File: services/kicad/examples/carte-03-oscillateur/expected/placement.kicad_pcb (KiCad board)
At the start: 2 copper layers, 27.8 x 19.8 mm, 15 parts, among them J1 PWR, J2 OUT, U1 NE555

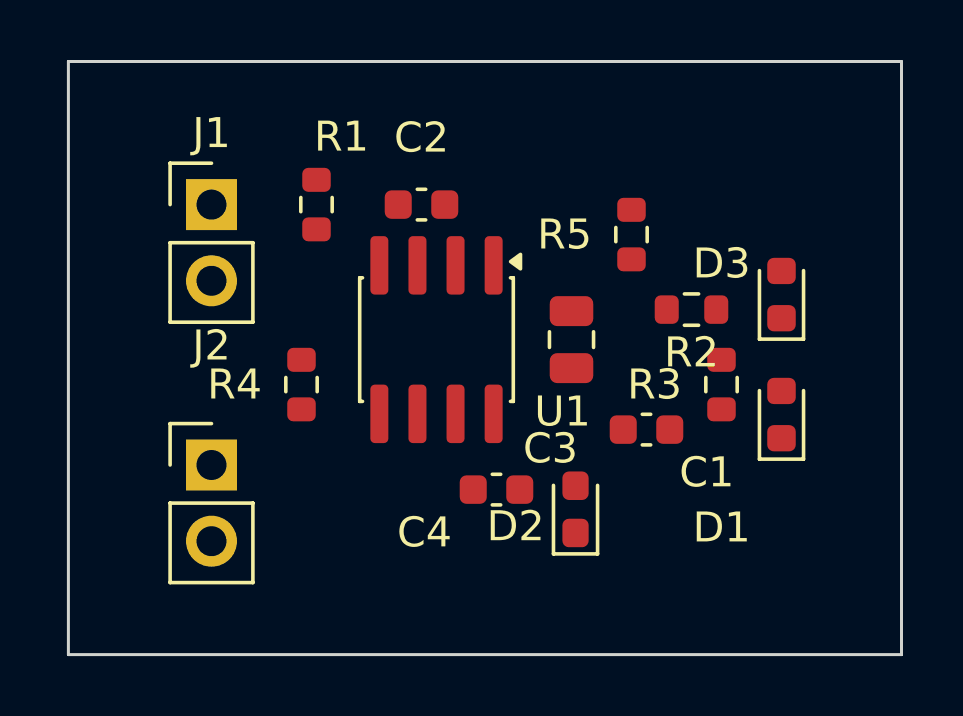
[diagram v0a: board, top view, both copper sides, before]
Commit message: feat(placement): les peripheriques se REPARTISSENT, ils ne s empilent plus
Question de l utilisateur devant le rendu : « c est quoi ce type de placement ? ».
Les composants s entassaient d un seul cote du boitier, etiquettes de
serigraphie l une sur l autre, trois quarts de la couronne vides.

TROIS CAUSES, toutes dans `_poser_les_peripheriques`, toutes la meme faute —
un angle unique pour tout un groupe :

  - les DIRECTS qui visent la meme broche (tous les decouplages d un rail,
    toutes les resistances d un meme signal) recevaient le MEME `angle_vers`
    et le meme rayon de depart ;
  - les SUIVEURS d un meme parent recevaient tous atan2(parent - centre) ;
  - les ISOLES partaient tous de l angle 0.0, c est-a-dire du meme point.

`le_long_du_rayon` ne s ecartait qu une fois la place prise : d ou la file.

REMEDE : `_ecart_en_eventail`. Le PREMIER de chaque groupe garde EXACTEMENT la
direction calculee — c est la topologie, on ne la perd pas pour faire joli — et
les suivants s ecartent symetriquement de 3 x `_PAS_ANGLE_DEG`.
Rien de deja pose ne bouge : seul l ANGLE DE DEPART de la recherche change, et
`le_long_du_rayon` reste seul juge de ce qui est libre.

BANC DES DIX CARTES, contour resserre ET peripheriques repartis :

    carte             demandee    livree         err  manq
    carte-01           25 x 20    20,1 x 13,6     0    0
    carte-02           55 x 40    34,9 x 25,2     0    0
    carte-03           50 x 35    27,6 x 19,9     0    0
    carte-04           60 x 45    36,6 x 29,8     0    0
    carte-05           70 x 50    40,0 x 32,6     0    0
    carte-06           80 x 60    46,5 x 36,4     0    0
    carte-07          110 x 80    47,7 x 38,8     0    0
    carte-08          125 x 95    57,4 x 44,1     0    0
    carte-09          130 x 100   57,8 x 45,2     0    0
    carte-10          140 x 105   59,0 x 45,8     0    0

Dix sur dix, 100 % route. carte-07 gagne 5,5 mm de largeur sur le passage
precedent, carte-06 deux, carte-10 deux. Sur ca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
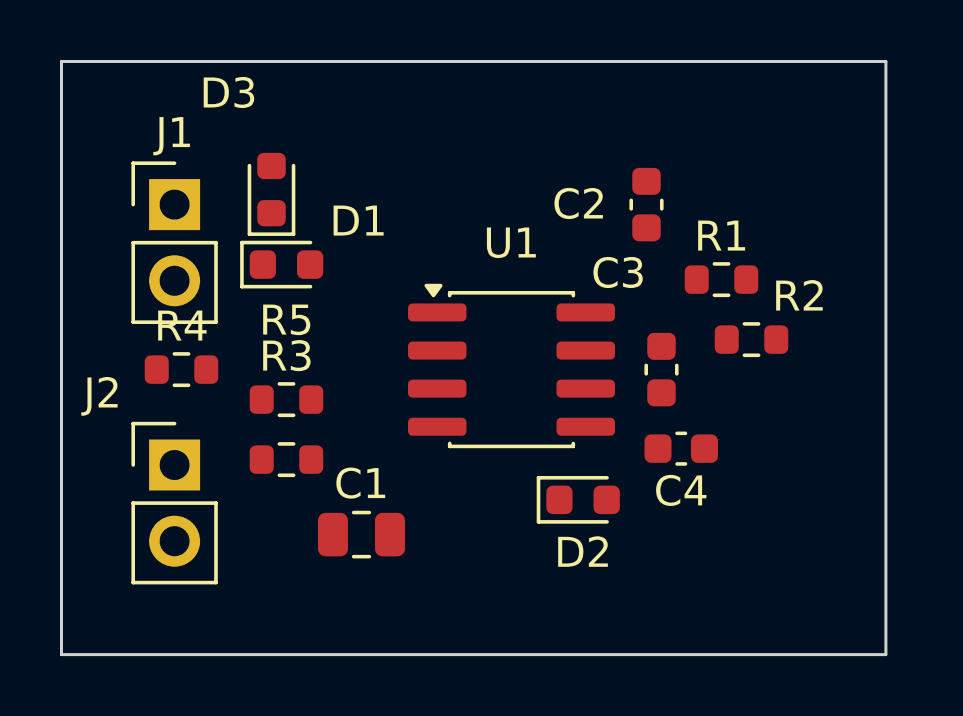
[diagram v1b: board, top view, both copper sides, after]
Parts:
- moved D3 17.4 mm to (130.5, 92.0)
- moved D1 17.2 mm to (131.0, 94.5), turned to 0 degrees
- moved R3 14.5 mm to (131.0, 99.0), turned to 0 degrees
- moved R1 13.7 mm to (145.5, 95.0), turned to 0 degrees
- moved R5 13.7 mm to (131.0, 101.0), turned to 0 degrees
- moved C1 9.55 mm to (133.5, 103.5), turned to 0 degrees
- moved C2 7.50 mm to (143.0, 92.5), turned to 90 degrees
- moved C4 6.31 mm to (144.2, 100.6)
- moved R4 4.03 mm to (127.5, 98.0), turned to 0 degrees
- moved U1 2.69 mm to (138.5, 98.0), turned to 0 degrees
- moved R2 2.24 mm to (146.5, 97.0), turned to 0 degrees
- moved C3 2.06 mm to (143.5, 98.0), turned to 90 degrees
- moved J1 1.23 mm to (127.3, 92.5)
- moved J2 1.23 mm to (127.3, 101.2)
- moved D2 0.40 mm to (140.9, 102.3), turned to 0 degrees
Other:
- board size 27.8 x 19.8 mm -> 27.5 x 19.8 mm

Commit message: docs(banc): les dix boards du banc du 2026-09-23, service corrige
Artefacts du banc dont le tableau est deja commite : les dix cartes a
100 % route, 0 erreur, 0 connexion manquante, chacune a la taille de son
circuit.

Co-Authored-By: Claude Opus 5 <noreply@anthropic.com>
Claude-Session: https://claude.ai/code/session_01TnMqm4La2CxQHHB5K8aSSV
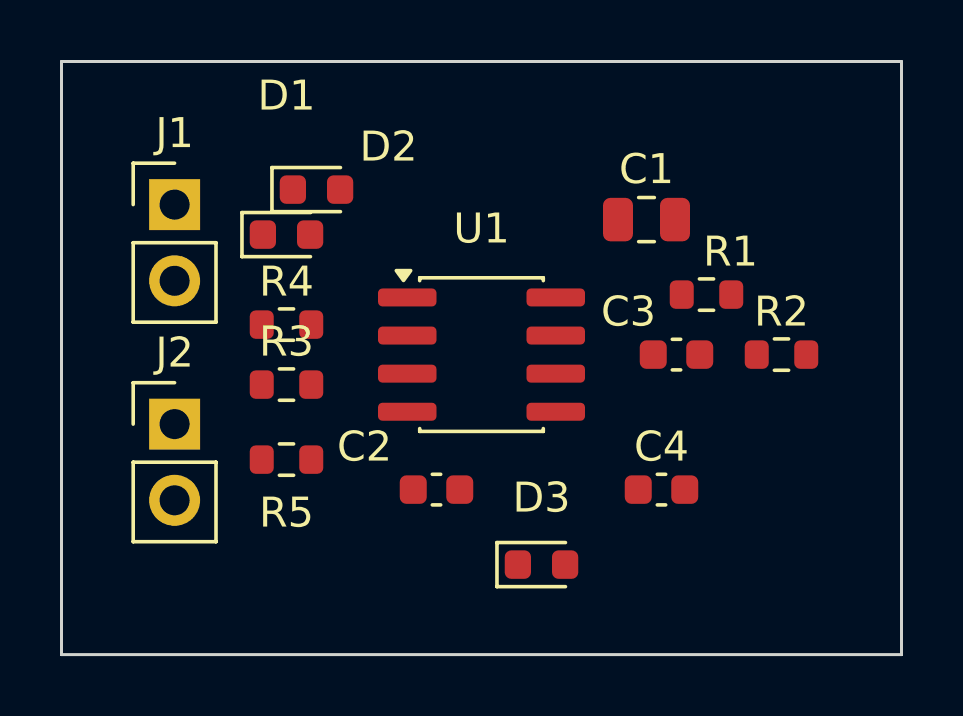
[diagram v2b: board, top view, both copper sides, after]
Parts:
- moved D3 15.4 mm to (139.5, 104.5), turned to 0 degrees
- moved C1 14.2 mm to (143.0, 93.0)
- moved D2 13.6 mm to (132.0, 92.0)
- moved C2 11.8 mm to (136.0, 102.0), turned to 0 degrees
- moved R4 3.81 mm to (131.0, 96.5)
- moved C4 1.52 mm to (143.5, 102.0), turned to 0 degrees
- moved J2 1.36 mm to (127.3, 99.8)
- moved R2 1.12 mm to (147.5, 97.5)
- moved U1 1.12 mm to (137.5, 97.5)
- moved D1 1.00 mm to (131.0, 93.5)
- moved C3 0.71 mm to (144.0, 97.5), turned to 0 degrees
- moved R1 0.71 mm to (145.0, 95.5)
- moved R3 0.50 mm to (131.0, 98.5)
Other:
- board size 27.5 x 19.8 mm -> 28 x 19.8 mm
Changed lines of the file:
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@@
 		(generator "kicad-footprint-generator")
 		(layer "F.Cu")
-		(at 127.27 92.5 0)
+		(at 127.27 92.5)
 		(descr "Through hole straight pin header, 1x02, 2.54mm pitch, single row")
 		(tags "Through hole pin header THT 1x02 2.54mm single row")
@@
 		(generator "kicad-footprint-generator")
 		(layer "F.Cu")
-		(at 138.5 98 0)
+		(at 137.5 97.5)
 		(descr "SOIC, 8 Pin (JEDEC MS-012AA, https://www.analog.com/media/en/package-pcb-resources/package/pkg_pdf/soic_narrow-r/r_8.pdf)")
 		(tags "SOIC SO")
@@
 		(generator "kicad-footprint-generator")
 		(layer "F.Cu")
-		(at 145.5 95 0)
+		(at 145 95.5)
 		(descr "Resistor SMD 0603 (1608 Metric), square (rectangular) end terminal, IPC-7351 nominal, (Body size source: IPC-SM-782 page 72, https://www.pcb-3d.com/wordpress/wp-content/uploads/ipc-sm-782a_amendment_1_and_2.pdf)")
 		(tags "resistor")
 		(property "Reference" "R1"
-			(at 0 -1.43 0)
+			(at 0.8 -1.43 0)
 			(layer "F.SilkS")
 			(effects
@@
 		(generator "kicad-footprint-generator")
 		(layer "F.Cu")
-		(at 146.5 97 0)
+		(at 147.5 97.5)
 		(descr "Resistor SMD 0603 (1608 Metric), square (rectangular) end terminal, IPC-7351 nominal, (Body size source: IPC-SM-782 page 72, https://www.pcb-3d.com/wordpress/wp-content/uploads/ipc-sm-782a_amendment_1_and_2.pdf)")
 		(tags "resistor")
 		(property "Reference" "R2"
-			(at 1.6 -1.43 0)
+			(at 0 -1.43 0)
 			(layer "F.SilkS")
 			(effects
@@
 		(generator "kicad-footprint-generator")
 		(layer "F.Cu")
-		(at 131 99 0)
+		(at 131 98.5)
 		(descr "Resistor SMD 0603 (1608 Metric), square (rectangular) end terminal, IPC-7351 nominal, (Body size source: IPC-SM-782 page 72, https://www.pcb-3d.com/wordpress/wp-content/uploads/ipc-sm-782a_amendment_1_and_2.pdf)")
 		(tags "resistor")
@@
 		(generator "kicad-footprint-generator")
 		(layer "F.Cu")
-		(at 127.5 98 0)
+		(at 131 96.5)
 		(descr "Resistor SMD 0603 (1608 Metric), square (rectangular) end terminal, IPC-7351 nominal, (Body size source: IPC-SM-782 page 72, https://www.pcb-3d.com/wordpress/wp-content/uploads/ipc-sm-782a_amendment_1_and_2.pdf)")
 		(tags "resistor")
@@
 		(generator "kicad-footprint-generator")
 		(layer "F.Cu")
-		(at 131 101 0)
+		(at 131 101)
 		(descr "Resistor SMD 0603 (1608 Metric), square (rectangular) end terminal, IPC-7351 nominal, (Body size source: IPC-SM-782 page 72, https://www.pcb-3d.com/wordpress/wp-content/uploads/ipc-sm-782a_amendment_1_and_2.pdf)")
 		(tags "resistor")
 		(property "Reference" "R5"
-			(at -5.8783e-16 -4.63 0)
+			(at 1.95943e-16 1.77 0)
 			(layer "F.SilkS")
 			(effects
@@
 		(generator "kicad-footprint-generator")
 		(layer "F.Cu")
-		(at 133.5 103.5 0)
+		(at 143 93)
 		(descr "Capacitor SMD 0805 (2012 Metric), square (rectangular) end terminal, IPC-7351 nominal, (Body size source: IPC-SM-782 page 76, https://www.pcb-3d.com/wordpress/wp-content/uploads/ipc-sm-782a_amendment_1_and_2.pdf, https://docs.google.com/spreadsheets/d/1BsfQQcO9C6DZCsRaXUlFlo91Tg2WpOkGARC1WS5S8t0/edit?usp=sharing)")
 		(tags "capacitor")
@@
 		(generator "kicad-footprint-generator")
 		(layer "F.Cu")
-		(at 143 92.5 90)
+		(at 136 102)
 		(descr "Capacitor SMD 0603 (1608 Metric), square (rectangular) end terminal, IPC-7351 nominal, (Body size source: IPC-SM-782 page 76, https://www.pcb-3d.com/wordpress/wp-content/uploads/ipc-sm-782a_amendment_1_and_2.pdf)")
 		(tags "capacitor")
 		(property "Reference" "C2"
-			(at -1.46958e-16 -2.23 0)
+			(at -2.4 -1.43 0)
 			(layer "F.SilkS")
 			(effects
@@
 		)
 		(pad "1" smd roundrect
-			(at -0.775 0 90)
+			(at -0.775 0)
 			(size 0.9 0.95)
 			(layers "F.Cu" "F.Mask" "F.Paste")
@@
 		)
 		(pad "2" smd roundrect
-			(at 0.775 0 90)
+			(at 0.775 0)
 			(size 0.9 0.95)
 			(layers "F.Cu" "F.Mask" "F.Paste")
@@
 		(generator "kicad-footprint-generator")
 		(layer "F.Cu")
-		(at 143.5 98 90)
+		(at 144 97.5)
 		(descr "Capacitor SMD 0603 (1608 Metric), square (rectangular) end terminal, IPC-7351 nominal, (Body size source: IPC-SM-782 page 76, https://www.pcb-3d.com/wordpress/wp-content/uploads/ipc-sm-782a_amendment_1_and_2.pdf)")
 		(tags "capacitor")
 		(property "Reference" "C3"
-			(at 3.2 -1.43 0)
+			(at -1.6 -1.43 0)
 			(layer "F.SilkS")
 			(effects
@@
 		)
 		(pad "1" smd roundrect
-			(at -0.775 0 90)
+			(at -0.775 0)
 			(size 0.9 0.95)
 			(layers "F.Cu" "F.Mask" "F.Paste")
@@
 		)
 		(pad "2" smd roundrect
-			(at 0.775 0 90)
+			(at 0.775 0)
 			(size 0.9 0.95)
 			(layers "F.Cu" "F.Mask" "F.Paste")
@@
 		(generator "kicad-footprint-generator")
 		(layer "F.Cu")
-		(at 144.1585 100.6342 180)
+		(at 143.5 102)
 		(descr "Capacitor SMD 0603 (1608 Metric), square (rectangular) end terminal, IPC-7351 nominal, (Body size source: IPC-SM-782 page 76, https://www.pcb-3d.com/wordpress/wp-content/uploads/ipc-sm-782a_amendment_1_and_2.pdf)")
 		(tags "capacitor")
@@
 		)
 		(pad "1" smd roundrect
-			(at -0.775 0 180)
+			(at -0.775 0)
 			(size 0.9 0.95)
 			(layers "F.Cu" "F.Mask" "F.Paste")
@@
 		)
 		(pad "2" smd roundrect
-			(at 0.775 0 180)
+			(at 0.775 0)
 			(size 0.9 0.95)
 			(layers "F.Cu" "F.Mask" "F.Paste")
@@
 		(generator "kicad-footprint-generator")
 		(layer "F.Cu")
-		(at 131 94.5 0)
+		(at 131 93.5)
 		(descr "LED SMD 0603 (1608 Metric), square (rectangular) end terminal, IPC-7351 nominal, (Body size source: http://www.tortai-tech.com/upload/download/2011102023233369053.pdf)")
 		(tags "LED")
 		(property "Reference" "D1"
-			(at 2.4 -1.43 0)
+			(at -5.8783e-16 -4.63 0)
 			(layer "F.SilkS")
 			(effects
@@
 		(generator "kicad-footprint-generator")
 		(layer "F.Cu")
-		(at 140.8858 102.3414 0)
+		(at 132 92)
 		(descr "LED SMD 0603 (1608 Metric), square (rectangular) end terminal, IPC-7351 nominal, (Body size source: http://www.tortai-tech.com/upload/download/2011102023233369053.pdf)")
 		(tags "LED")
 		(property "Reference" "D2"
-			(at 1.95943e-16 1.77 0)
+			(at 2.4 -1.43 0)
 			(layer "F.SilkS")
 			(effects
@@
 		(generator "kicad-footprint-generator")
 		(layer "F.Cu")
-		(at 130.5 92 90)
+		(at 139.5 104.5)
 		(descr "LED SMD 0603 (1608 Metric), square (rectangular) end terminal, IPC-7351 nominal, (Body size source: http://www.tortai-tech.com/upload/download/2011102023233369053.pdf)")
 		(tags "LED")
 		(property "Reference" "D3"
-			(at 3.2 -1.43 0)
+			(at -1.46958e-16 -2.23 0)
 			(layer "F.SilkS")
 			(effects
@@
 		)
 		(pad "1" smd roundrect
-			(at -0.7875 0 90)
+			(at -0.7875 0)
 			(size 0.875 0.95)
 			(layers "F.Cu" "F.Mask" "F.Paste")
@@
 		)
 		(pad "2" smd roundrect
-			(at 0.7875 0 90)
+			(at 0.7875 0)
 			(size 0.875 0.95)
 			(layers "F.Cu" "F.Mask" "F.Paste")
@@
 		(generator "kicad-footprint-generator")
 		(layer "F.Cu")
-		(at 127.27 101.18 0)
+		(at 127.27 99.8169)
 		(descr "Through hole straight pin header, 1x02, 2.54mm pitch, single row")
 		(tags "Through hole pin header THT 1x02 2.54mm single row")
 		(property "Reference" "J2"
-			(at -2.4 -2.38 0)
+			(at 0 -2.38 0)
 			(layer "F.SilkS")
 			(effects
@@
 	(gr_rect
 		(start 123.500 87.730)
-		(end 150.980 107.500)
+		(end 151.500 107.500)
 		(stroke
 			(width 0.1)
